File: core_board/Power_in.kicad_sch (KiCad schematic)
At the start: 35 parts, among them J1 Molex_Megafit_02, Q1 TPC8132_LQS, U1 AP63301WU7, U2 AP63205QWU7, U4 BD9G401EFJ-E2

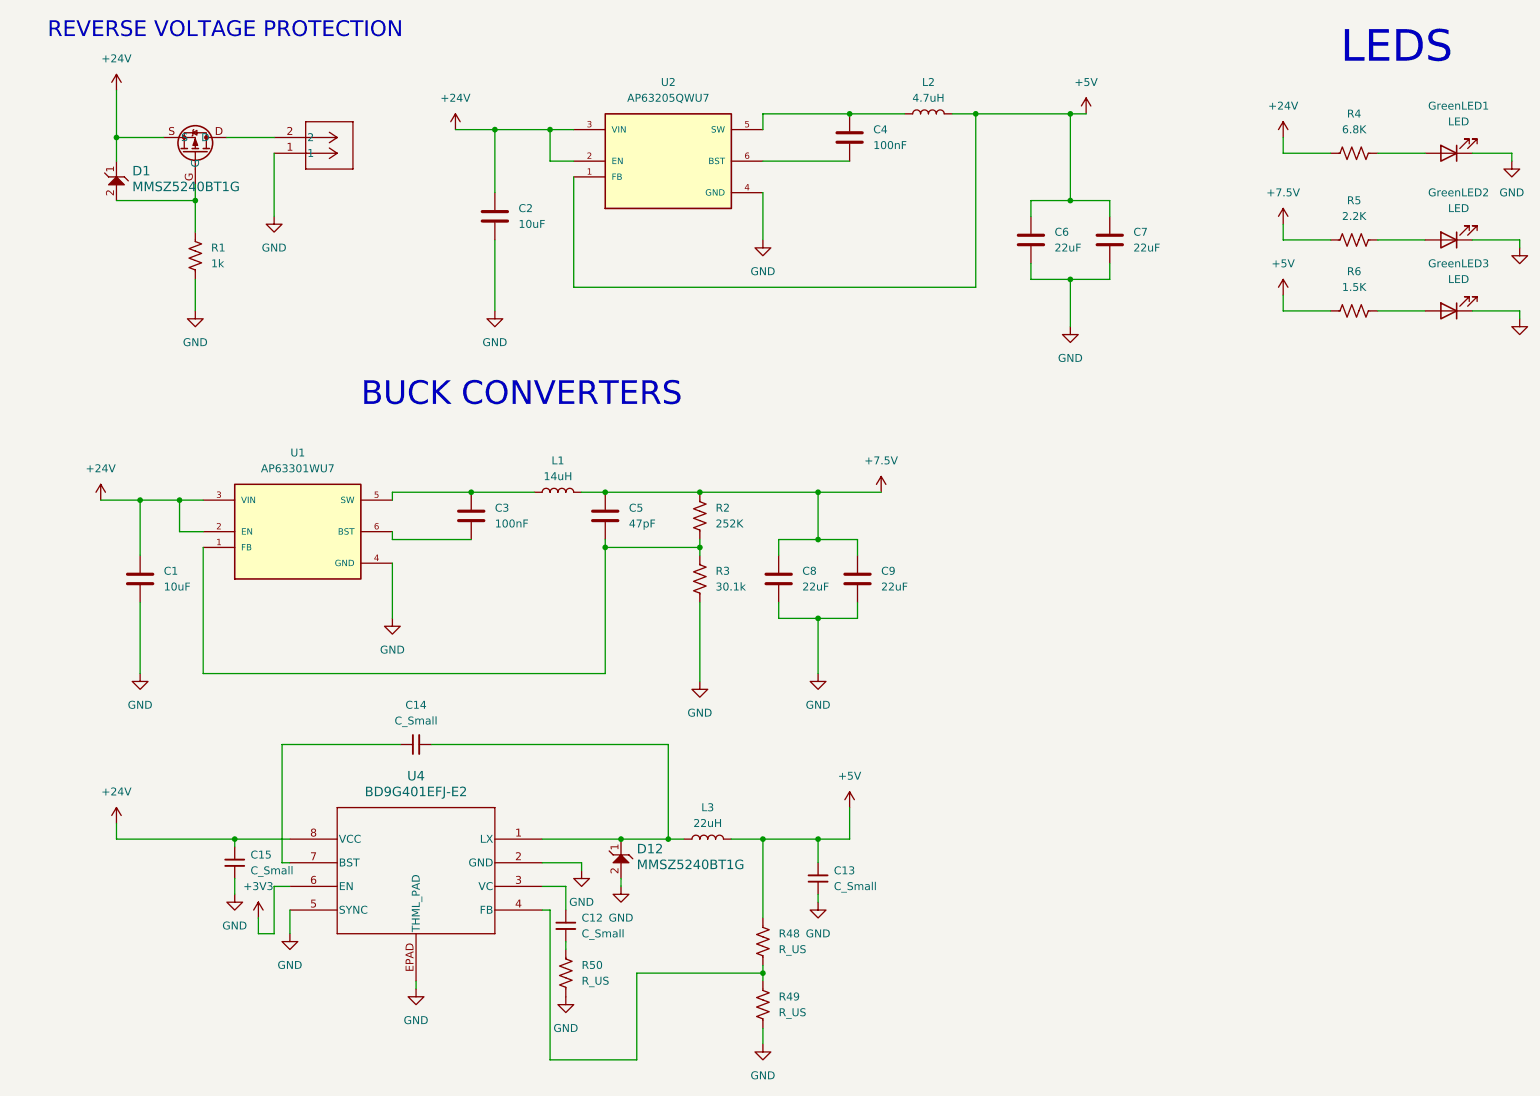
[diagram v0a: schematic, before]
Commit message: Add extra components
fixed LED connector
removed extra buck
fixed wrong footprints
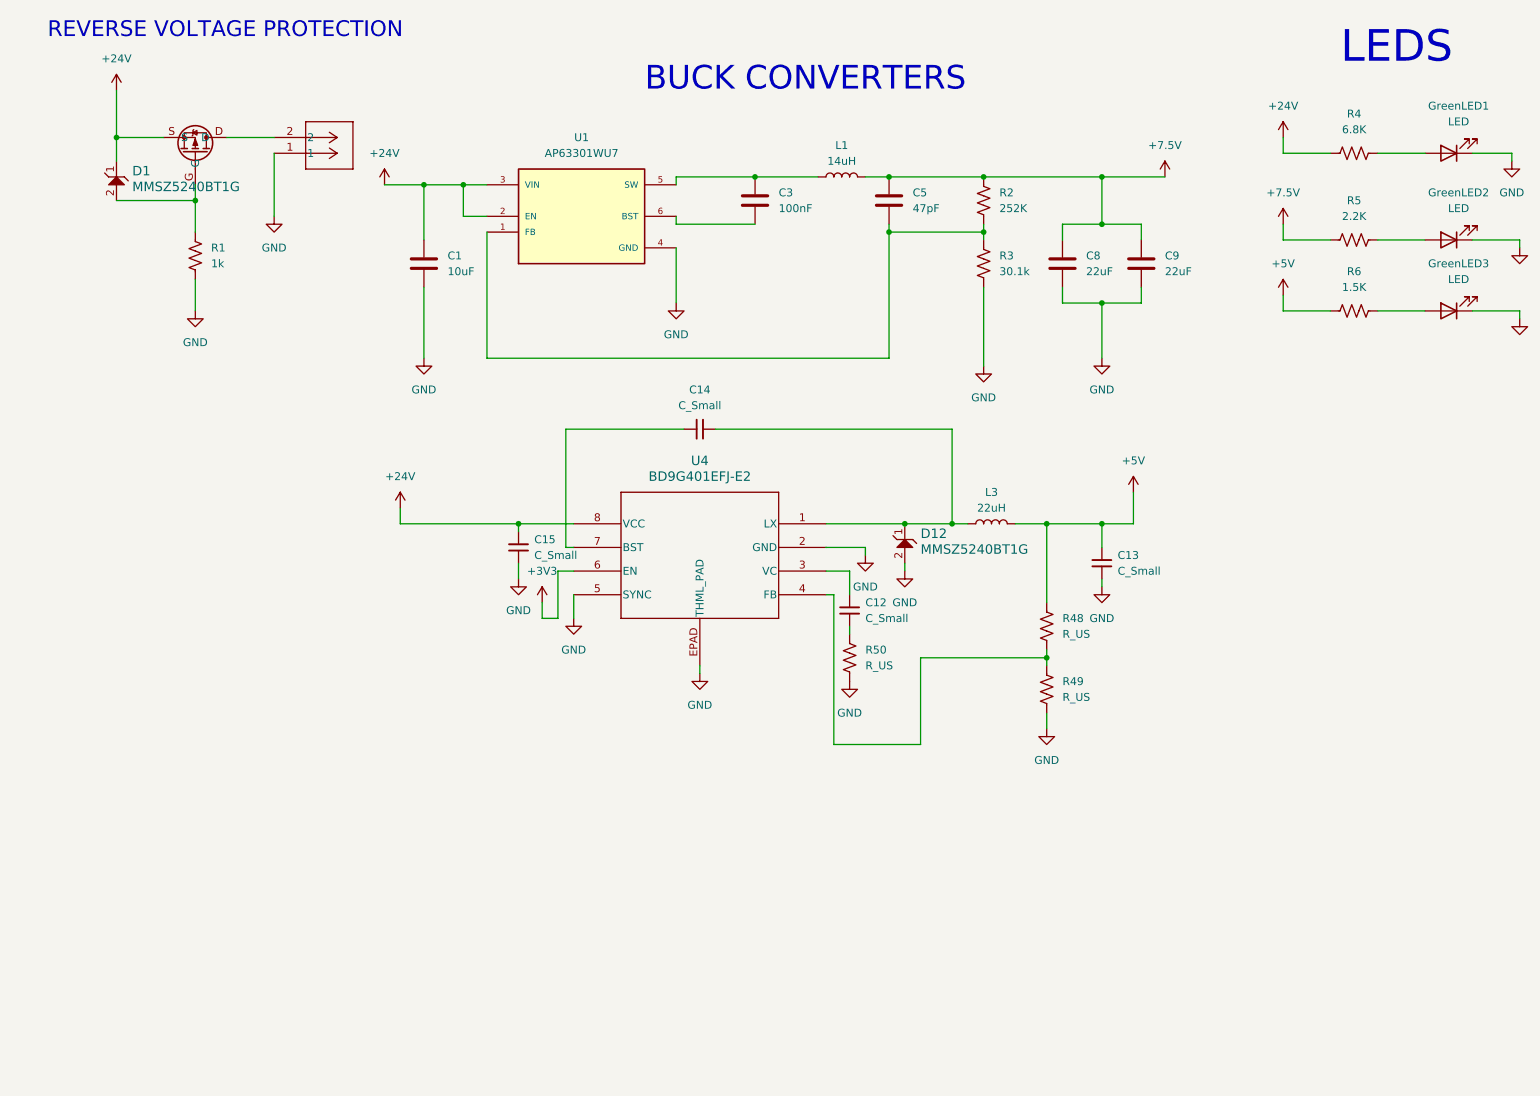
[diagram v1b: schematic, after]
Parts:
- removed C2: 10uF, Capacitor_SMD:C_0603_1608Metric_Pad1.08x0.95mm_HandSolder, symbol Device:C
- removed C4: 100nF, Capacitor_SMD:C_0603_1608Metric_Pad1.08x0.95mm_HandSolder, symbol Device:C
- removed C6, C7: 22uF, Capacitor_SMD:C_0603_1608Metric_Pad1.08x0.95mm_HandSolder, symbol Device:C
- removed L2: 4.7uH, Inductor_SMD:L_0603_1608Metric, symbol Device:L
- removed U2: AP63205QWU7, Package_TO_SOT_SMD:SOT-23-6_Handsoldering, symbol AP63205QWU7:AP63205QWU7
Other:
- moved on the sheet: C1, C12, C13, C14, C15, C3, C5, C8, C9, D12, L1, L3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

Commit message: Layout updates
footprint changes
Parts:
- J1: footprint MRDT_Connectors:MOLEX_MegaFit_02_Horizontal -> MRDT_Connectors:MOLEX_MegaFit_02_Vertical

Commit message: add
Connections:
- net SW: now reaches C3.1, L1.1, U1.5 (SW)
- net BST: now reaches C3.2, U1.6 (BST)

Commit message: Fix buck circuit values
nothing had values, so I added them
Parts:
- C12: value C_Small -> 0.01uF
- C13: value C_Small -> 47uF
- C14: value C_Small -> 0.1uF
- C15: value C_Small -> 10uF
- D12: value MMSZ5240BT1G -> PMEG4050EP,115; footprint LED_SMD:LED_0603_1608Metric_Pad1.05x0.95mm_HandSolder -> Diode_SMD:D_SOD-128
- R48: value R_US -> 160k
- R49: value R_US -> 30k
- R50: value R_US -> 4.7k
